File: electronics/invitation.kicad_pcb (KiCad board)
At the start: 2 copper layers, 86 x 57 mm, 63 parts, among them P1 USB Micro B, P10 Tassimo, P11 Maker, P2 James Miller, P3 CONN_02X03, P4 D&AD, P5 Krispy Kreme, P6 Epic Mind Drive, P7 Hacky Xmas, P8 Pay@Pump, P9 WIYWI, U1 ATMEGA32U4-A, Y1 16 FA-238 Mhz

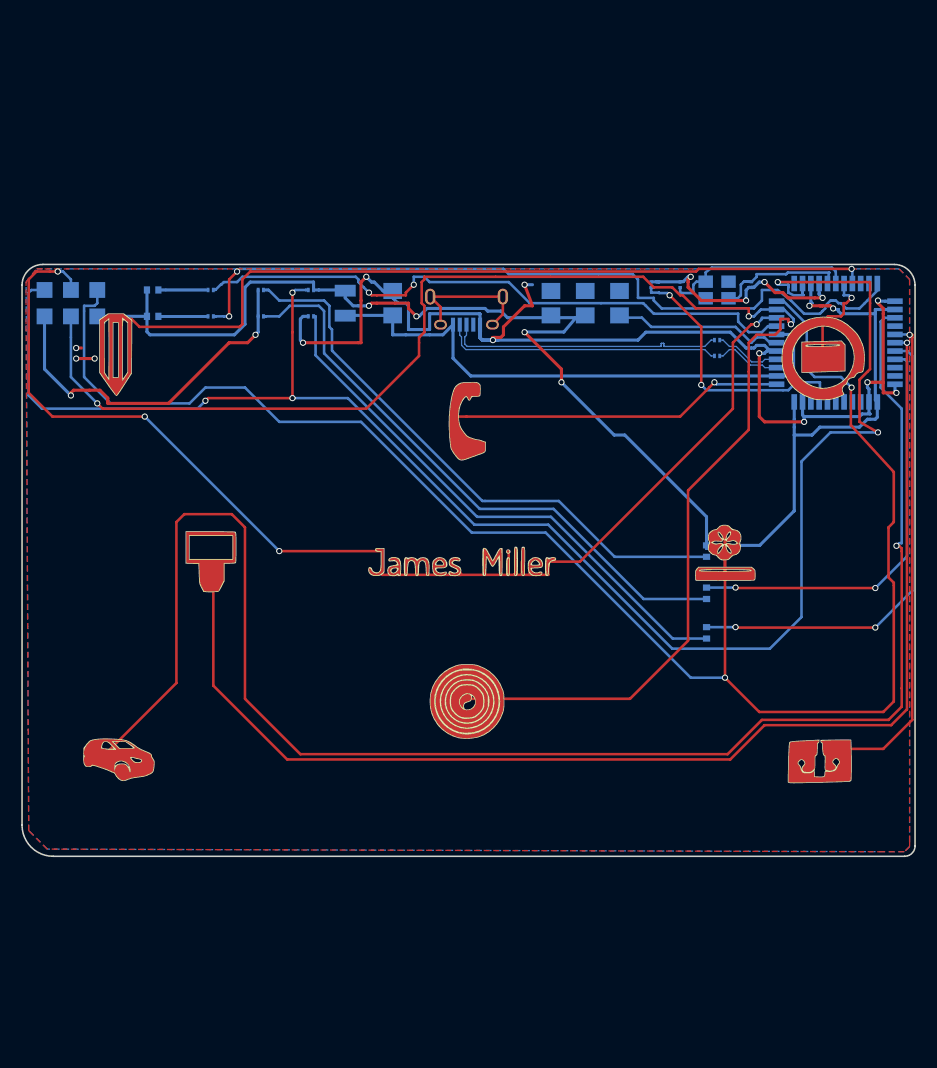
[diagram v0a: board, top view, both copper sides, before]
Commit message: Commit 51: Re-adjusted Gerber files for production (silk screen layers too small + logo and maker project gifs needed resizing)
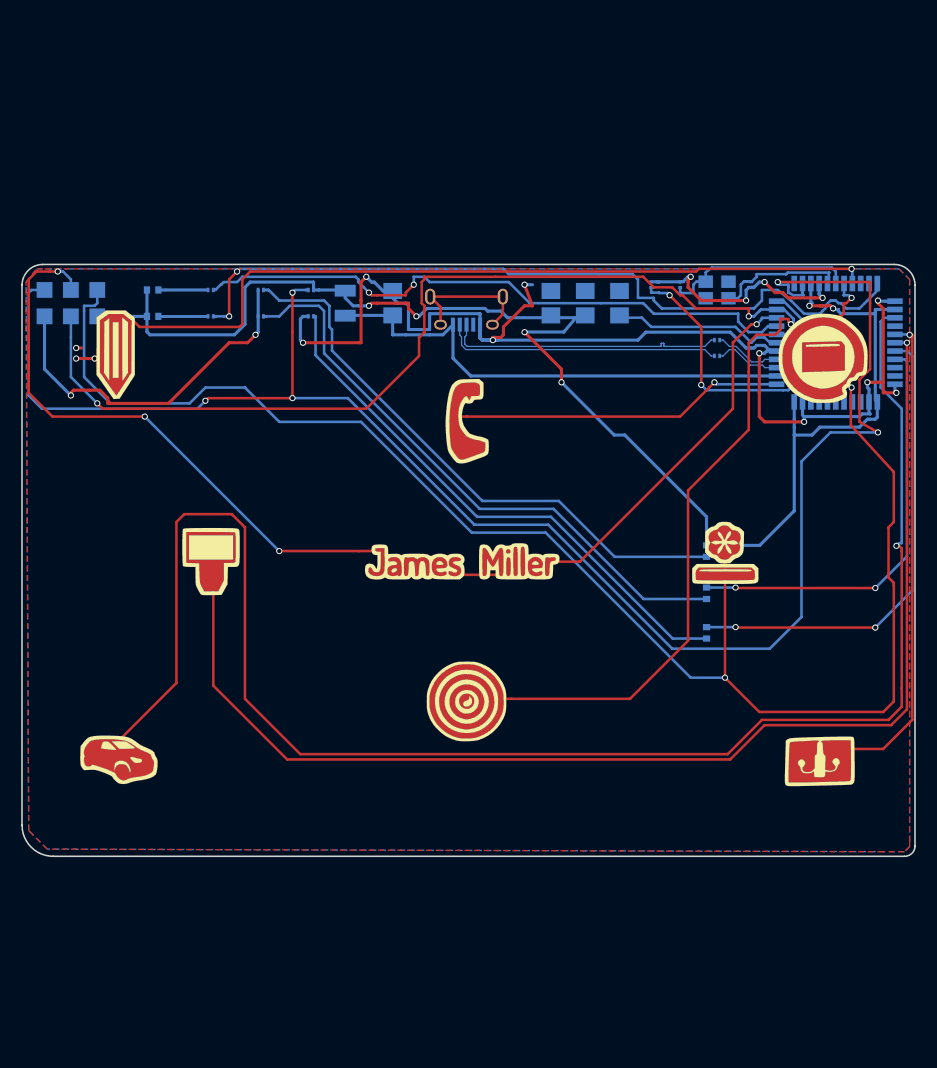
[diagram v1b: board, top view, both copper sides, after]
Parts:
- removed the P2 at (161.8, 99.8)
- added G***: LOGO, assets:JMLogo-F.Mask, F.Cu at (161.8, 99.8)
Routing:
- net SCLK: track 125.7 -> 138.2 mm
- net MOSI: track 155.8 -> 152.5 mm

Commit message: Electronics
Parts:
- removed C1: 1uF, Capacitors_Tantalum_SMD:CP_Tantalum_Case-R_EIA-2012-12_Reflow
- removed the G*** at (196.3, 80.3) (x3)
- removed the G*** at (186.9, 99.3) (x3)
- removed the G*** at (128.3, 79.8) (x3)
- removed the G*** at (162.1, 86.4) (x3)
- removed the G*** at (128.5, 118.9) (x3)
- removed the G*** at (162.1, 113.3) (x3)
- removed the G*** at (137.4, 99.8) (x3)
- removed the G*** at (196.1, 119.1) (x3)
- removed the G*** at (161.8, 99.8) (x2)
- removed P10: Tassimo, assets:tassimoGif
- removed P11: Maker, assets:makerGif
- removed the P2 at (161.8, 99.8) (x2)
- removed P9: WIYWI, assets:WIYWI
- added D6: TX LED (orange), LEDs:LED_0402, F.Cu at (149.6, 138.7)
- added D7: RX LED (orange), LEDs:LED_0402, F.Cu at (162.2, 138.3)
- added G***: LOGO, newAssets:JMDesignSS, F.Cu at (162.1, 99.6)
- added G***: LOGO, newAssets:leftArrowSS, F.Cu at (130.0, 99.8)
- added G***: LOGO, newAssets:rightArrowSS, F.Cu at (193.3, 99.8)
- added G***: LOGO, newAssets:JMDesignFMask, F.Cu at (162.1, 99.6)
- added G***: LOGO, newAssets:leftArrowFMask, F.Cu at (130.0, 99.8)
- added G***: LOGO, newAssets:rightArrowFMask, F.Cu at (193.3, 99.8)
- added P2: Home button, newAssets:JMDesign, F.Cu at (162.1, 99.6)
- added R10: 330, Resistors_SMD:R_0402, F.Cu at (174.5, 133.1)
- added R9: 330, Resistors_SMD:R_0402, F.Cu at (154.9, 145.8)
- C2, C3, C4, C5, C6, C7, D1, F1, Y1: moved to F.Cu
- D2: value Interaction LED (green) -> Website CTA (green); moved to F.Cu
- D3: value Node LED (green) -> Interaction LED (green); moved to F.Cu
- D4: value TX LED (orange) -> Phone LED (green); moved to F.Cu
- D5: value RX LED (orange) -> Email LED (green); moved to F.Cu
- P3: value CONN_02X03 -> Bottom Connections 1; footprint assets:Programming_port -> Connectors_Samtec:SL-103-X-XX_1x03; moved to F.Cu
- P4: value D&AD -> Left Arrow; footprint assets:moodTreeGif -> newAssets:leftArrow
- P5: value Krispy Kreme -> Right Arrow; footprint assets:krispyKreme -> newAssets:rightArrow
- P6: value Epic Mind Drive -> Right Connectors; footprint assets:mindDrive-F.Paste -> newAssets:SL-105-X-XX_1x05
- P7: value Hacky Xmas -> Left Connectors; footprint assets:hackyXmas -> newAssets:SL-105-X-XX_1x05
- P8: value Pay@Pump -> Bottom Connections 2; footprint assets:beerGif-F.Paste -> Connectors_Samtec:SL-103-X-XX_1x03
- R1, R2, R3, R4, R5, R6, R7, R8: footprint Resistors_SMD:R_0201 -> Resistors_SMD:R_0402; moved to F.Cu
- moved D4 78.2 mm to (167.9, 145.5), turned to 0 degrees
- moved P6 77.6 mm to (202.2, 94.5)
- moved P7 77.6 mm to (122.4, 94.7)
- moved R3 77.3 mm to (175.5, 145.5)
- moved D5 74.0 mm to (149.4, 145.5), turned to 0 degrees
- moved R4 69.8 mm to (167.6, 138.7), turned to 0 degrees
- moved R7 68.6 mm to (175.3, 138.7), turned to 0 degrees
- moved R5 67.0 mm to (155.4, 138.2), turned to 0 degrees
- moved R6 65.6 mm to (169.2, 133.6)
- moved R8 57.2 mm to (154.7, 132.1), turned to 0 degrees
- moved P3 50.2 mm to (130.8, 123.7), turned to 90 degrees
- moved P8 48.3 mm to (193.0, 123.4), turned to 90 degrees
- moved D1 47.1 mm to (188.2, 51.8), turned to 270 degrees
- moved D3 45.8 mm to (161.8, 146.1), turned to 0 degrees
- moved D2 39.3 mm to (161.0, 133.9), turned to 0 degrees
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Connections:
- net Net-(C3-Pad1) renamed XTal1
- net Net-(C5-Pad1) renamed XTal2
- D2 pad 2: interactLED -> nodeLED
- D3 pad 2: nodeLED -> interactLED
- D4 pad 2: VCC -> phoneLED
- D5 pad 2: VCC -> emailLED
- P4 pad 1: portfolio1Btn -> leftArrow
- P5 pad 1: portfolio2Btn -> rightArrow
- P6 pad 1: portfolio3Btn -> D0
- P7 pad 1: portfolio4Btn -> GND
- P8 pad 1: portfolio5Btn -> MOSI
- R5 pad 1: Net-(R5-Pad1) -> TXLED
- R5 pad 2: Net-(D5-Pad1) -> Net-(D7-Pad1)
- R6 pad 1: Net-(D4-Pad1) -> RXLED
- R6 pad 2: Net-(R6-Pad2) -> Net-(D6-Pad1)
- R7 pad 1: Net-(D3-Pad1) -> Net-(D2-Pad1)
- R8 pad 1: Net-(D2-Pad1) -> Net-(D3-Pad1)
- U1 pad 1: portfolio5Btn -> Net-(U1-Pad1)
- U1 pad 18: portfolio2Btn -> D3
- U1 pad 19: portfolio1Btn -> D2
- U1 pad 20: Net-(U1-Pad20) -> D0
- U1 pad 21: Net-(U1-Pad21) -> D1
- U1 pad 22: Net-(R6-Pad2) -> TXLED
- U1 pad 25: portfolio3Btn -> D4
- U1 pad 27: portfolio4Btn -> Net-(U1-Pad27)
- U1 pad 28: portfolio6Btn -> Net-(U1-Pad28)
- U1 pad 31: Net-(U1-Pad31) -> phoneLED
- U1 pad 32: Net-(U1-Pad32) -> emailLED
- U1 pad 36: Net-(U1-Pad36) -> A0
- U1 pad 37: Net-(U1-Pad37) -> A1
- U1 pad 38: Net-(U1-Pad38) -> A2
- U1 pad 39: Net-(U1-Pad39) -> rightArrow
- U1 pad 40: Net-(U1-Pad40) -> leftArrow
- U1 pad 41: Net-(U1-Pad41) -> homeBtn
- U1 pad 8: Net-(R5-Pad1) -> RXLED
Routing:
- net GND: track 171.8 -> 0.00 mm, vias 15 -> 0
- net MISO: track 167.0 -> 0.00 mm, vias 2 -> 0
- net RESET: track 164.4 -> 0.00 mm, vias 5 -> 0
- net portfolio3Btn: track 157.7 -> 0.00 mm, vias 1 -> 0
- net MOSI: track 152.5 -> 0.00 mm, vias 3 -> 0
- net VCC: track 144.9 -> 0.00 mm, vias 6 -> 0
- net SCLK: track 138.2 -> 0.00 mm, vias 4 -> 0
- net portfolio6Btn: track 119.6 -> 0.00 mm, vias 1 -> 0
- net portfolio1Btn: track 77.7 -> 0.00 mm, vias 1 -> 0
- net Net-(R6-Pad2): track 75.3 -> 0.00 mm, vias 2 -> 0
- net Net-(R5-Pad1): track 60.0 -> 0.00 mm, vias 2 -> 0
- net Net-(D2-Pad1): track 57.2 -> 0.00 mm
- net Net-(D1-Pad1): track 56.0 -> 0.00 mm
- net USBVCC: track 55.2 -> 0.00 mm
- net Net-(D3-Pad1): track 52.9 -> 0.00 mm
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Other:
- board text added: "@"
- board text added: "Connect this card to your PC with a USB cable Open in a web browser Tap the silver icons on this card's reverse side"
- board text added: "Get in touch"
- board text added: "How to play:"
- board text added: "Say"
- board text added: "hi"
- board text added: "jamesmiller.design"
- board text added: "www.jamesmiller.design"
- board text removed: "Connect this card to your PC with the USB cable Open in a web browser Tap the buttons on the reverse side to explore"
- board text removed: "GND"
- board text removed: "How to access James' portfolio:"
- board text removed: "MISO"
- board text removed: "MOSI"
- board text removed: "RESET"
- board text removed: "SCLK"
- board text removed: "VCC"
- board text removed: "info@jamesmillerportfolio.co.uk"
- board text removed: "www.jamesmillerportfolio.co.uk"
